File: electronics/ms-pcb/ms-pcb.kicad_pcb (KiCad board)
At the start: 2 copper layers, 112.5 x 110 mm, 16 parts, among them J1 Left motor, J2 Right motor, J3 XT60-M

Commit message: elec: start PCB layout
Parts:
- added H1: Motor_holes, footprints:Polulu_Micro_Gearmotor, F.Cu at (100.0, 95.0)
- added H2: Caster_wheel_holes, footprints:caster_wheel, F.Cu at (133.0, 51.0)
- added H3: Motor_holes, footprints:Polulu_Micro_Gearmotor, F.Cu at (167.0, 95.0)
- added H4: Caster_wheel_holes, footprints:caster_wheel, F.Cu at (133.0, 139.0)
- added S1: PTS526_SMG15_SMTR2_LFS, footprints:SW_PTS526_SMG15_SMTR2_LFS, F.Cu at (135.0, 95.0)
- added U1: ESP32-S3-DEVKITC-1U-N8R2, footprints:XCVR_ESP32-S3-DEVKITC-1U-N8R2, F.Cu at (134.0, 73.0)
- added U2: GY-521, footprints:GY-521, B.Cu at (106.0, 122.0)
- LS1, R2, R5: moved to B.Cu
- VL53L1X1: value ToF distance sensor -> Left; footprint Connector_PinHeader_2.54mm:PinHeader_1x06_P2.54mm_Horizontal -> footprints:TinyTronics_VL53L1X
- VL53L1X2: value ToF distance sensor -> Front-right; footprint Connector_PinHeader_2.54mm:PinHeader_1x06_P2.54mm_Horizontal -> footprints:TinyTronics_VL53L1X
- VL53L1X3: value ToF distance sensor -> Front-left; footprint Connector_PinHeader_2.54mm:PinHeader_1x06_P2.54mm_Horizontal -> footprints:TinyTronics_VL53L1X
- VL53L1X4: value ToF distance sensor -> Right; footprint Connector_PinHeader_2.54mm:PinHeader_1x06_P2.54mm_Horizontal -> footprints:TinyTronics_VL53L1X
- VL53L1X5: value ToF distance sensor -> Front; footprint Connector_PinHeader_2.54mm:PinHeader_1x06_P2.54mm_Horizontal -> footprints:TinyTronics_VL53L1X
- moved J3 259.3 mm to (171.0, 122.0), turned to -90 degrees
- moved J2 239.3 mm to (160.0, 108.0), turned to 180 degrees
- moved VL53L1X2 237.3 mm to (178.6, 70.4), turned to -135 degrees
- moved D1 217.6 mm to (140.5, 109.0)
- moved R3 214.2 mm to (141.0, 103.0)
- moved VL53L1X4 210.7 mm to (151.7, 55.4), turned to 180 degrees
- moved D2 206.6 mm to (125.5, 109.0)
- moved R4 200.1 mm to (125.5, 103.0)
- moved R2 198.4 mm to (153.0, 70.0)
- moved VL53L1X5 180.9 mm to (139.8, 46.7), turned to -90 degrees
- moved R5 176.7 mm to (153.0, 76.0), turned to 180 degrees
- moved VL53L1X3 173.7 mm to (97.7, 61.2), turned to -45 degrees
- moved R1 167.5 mm to (125.0, 96.0), turned to 180 degrees
- moved LS1 164.5 mm to (120.0, 72.0), turned to 180 degrees
- moved J1 158.2 mm to (107.0, 108.0), turned to 180 degrees
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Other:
- board outline removed

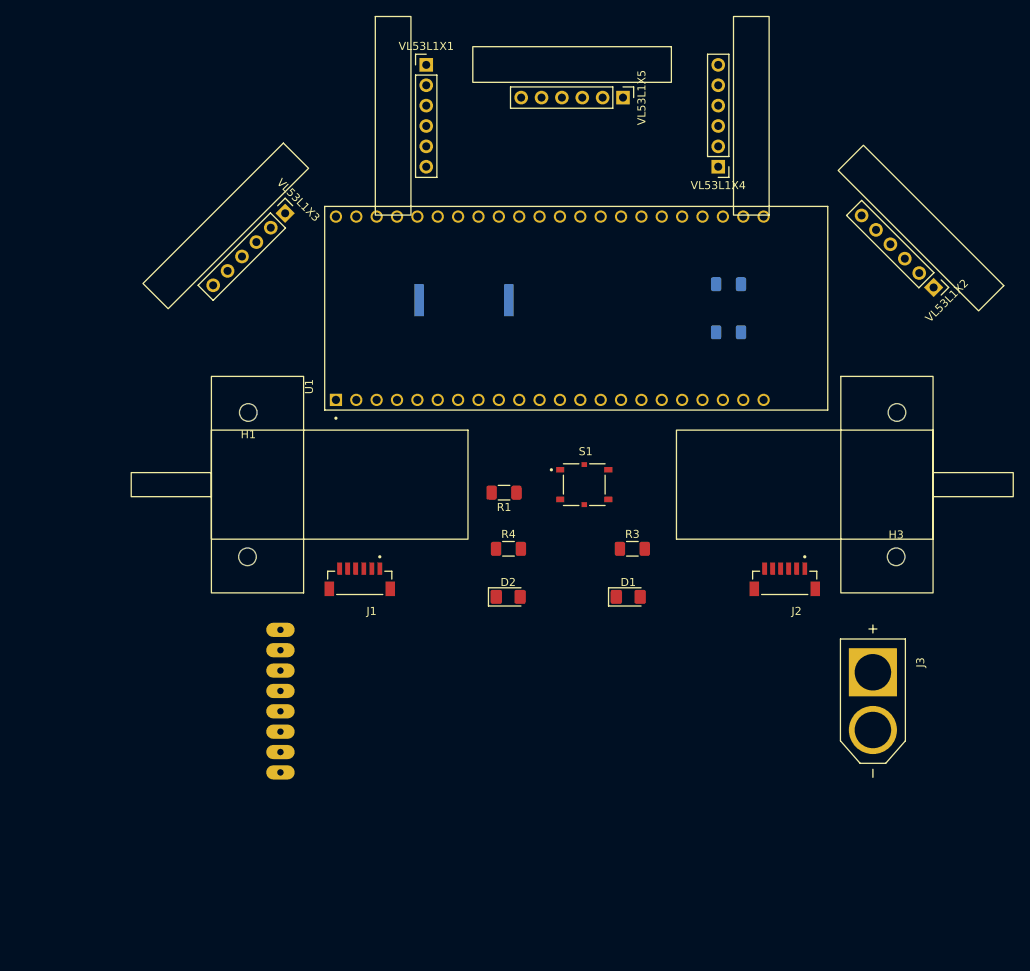
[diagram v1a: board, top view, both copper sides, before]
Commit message: elec: add more 3D and link them to footprints
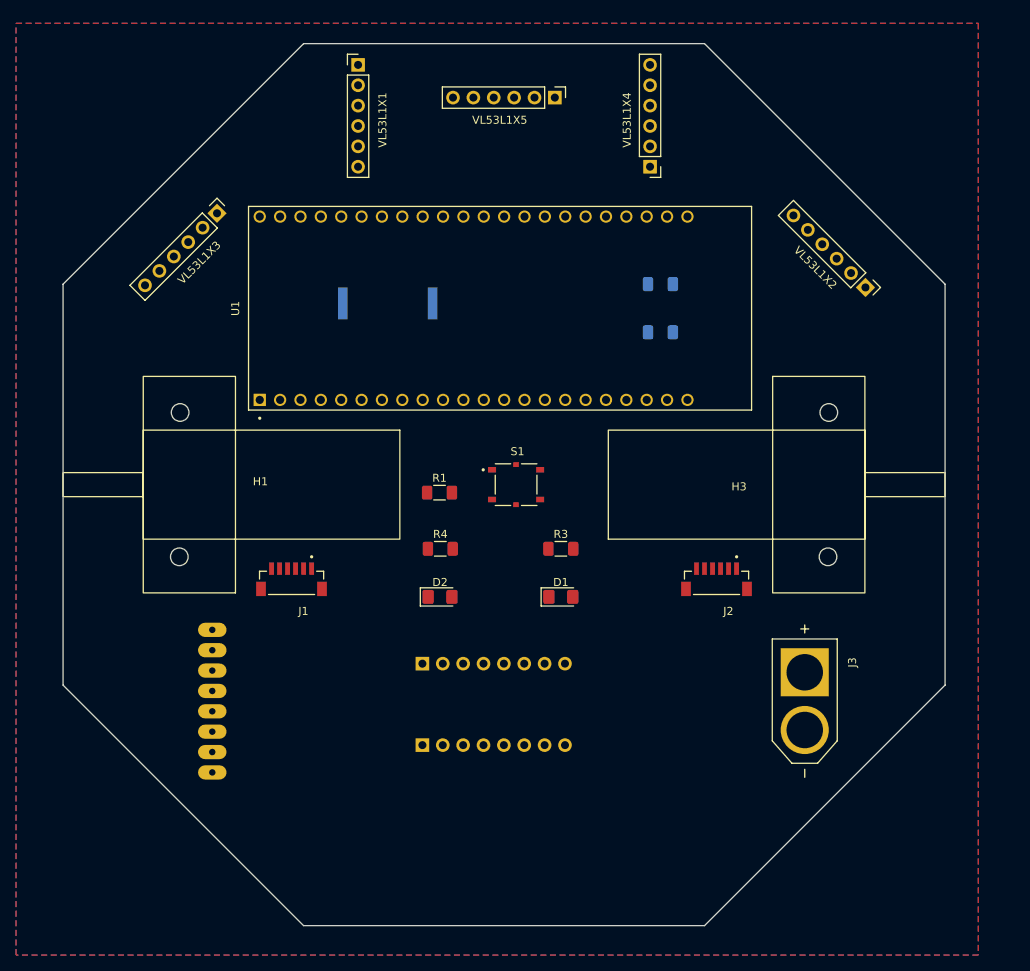
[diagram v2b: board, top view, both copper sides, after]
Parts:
- added DRV1: DRV8833, footprints:Polulu_DRV8833, B.Cu at (123.8, 122.6)
- R1: value 100k -> 20k
- moved LS1 9.52 mm to (110.5, 72.4)
- moved U1 9.50 mm to (124.5, 73.0)
- moved R3 8.92 mm to (132.1, 103.0)
- moved H3 8.50 mm to (158.5, 95.0)
- moved H1 8.50 mm to (91.5, 95.0)
- moved VL53L1X2 8.50 mm to (170.1, 70.4)
- moved VL53L1X1 8.50 mm to (106.8, 42.7)
- moved D2 8.50 mm to (117.0, 109.0)
- moved H2 8.50 mm to (124.5, 51.0)
- moved H4 8.50 mm to (124.5, 139.0)
- moved R2 8.50 mm to (144.5, 70.0)
- moved R4 8.50 mm to (117.0, 103.0)
- moved R5 8.50 mm to (144.5, 76.0)
- moved U2 8.50 mm to (97.5, 122.0)
- moved S1 8.50 mm to (126.5, 95.0)
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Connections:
- R1 pad 2: GND -> button
- R4 pad 1: +BATT -> +3.3V
- S1 pad 1: +3.3V -> button
- S1 pad 2: +3.3V -> button
- S1 pad 3: button -> GND
- S1 pad 4: button -> GND
- S1 pad G1: GND -> Net-(S1-PadG1)
- S1 pad G2: GND -> Net-(S1-PadG1)
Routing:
- added copper zone on F.Cu, net +3.3V
- added copper zone on B.Cu, net GND
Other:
- board outline added: 110 x 110 mm

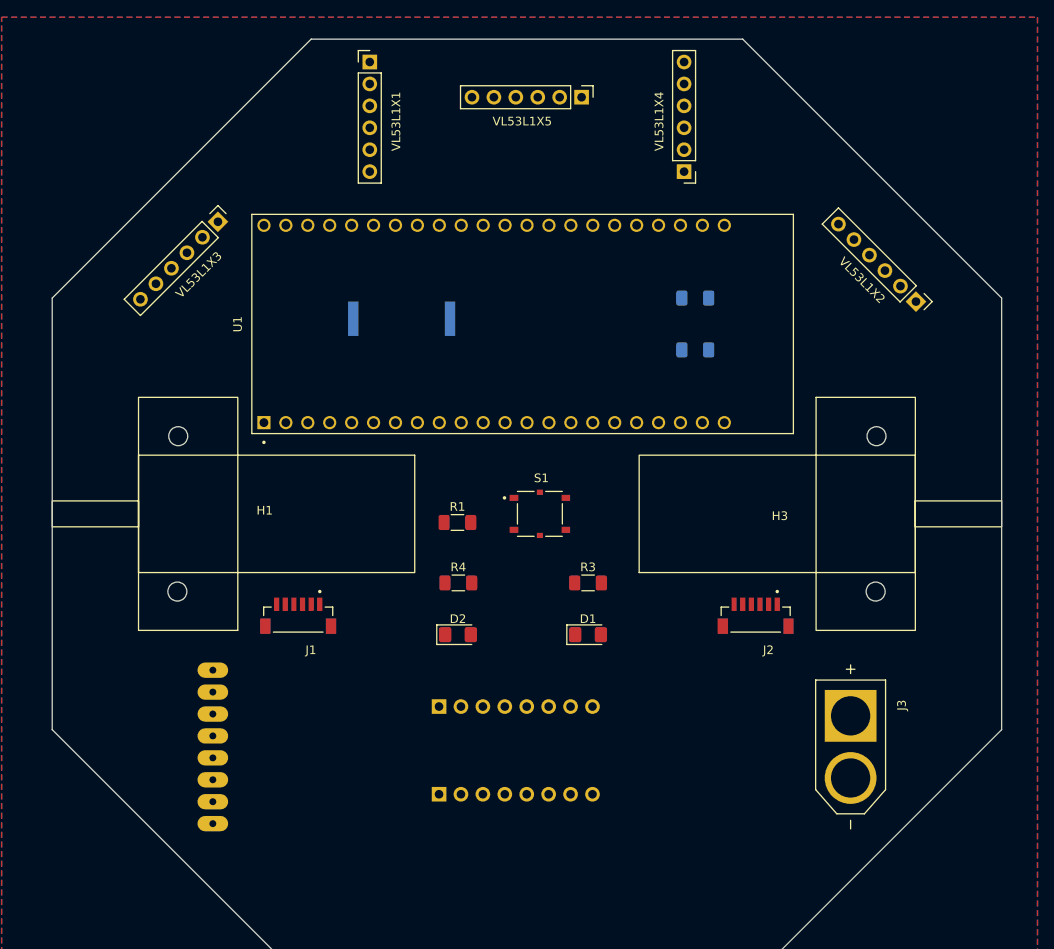
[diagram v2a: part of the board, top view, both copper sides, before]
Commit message: elec: add most 3D models
Closes: #19
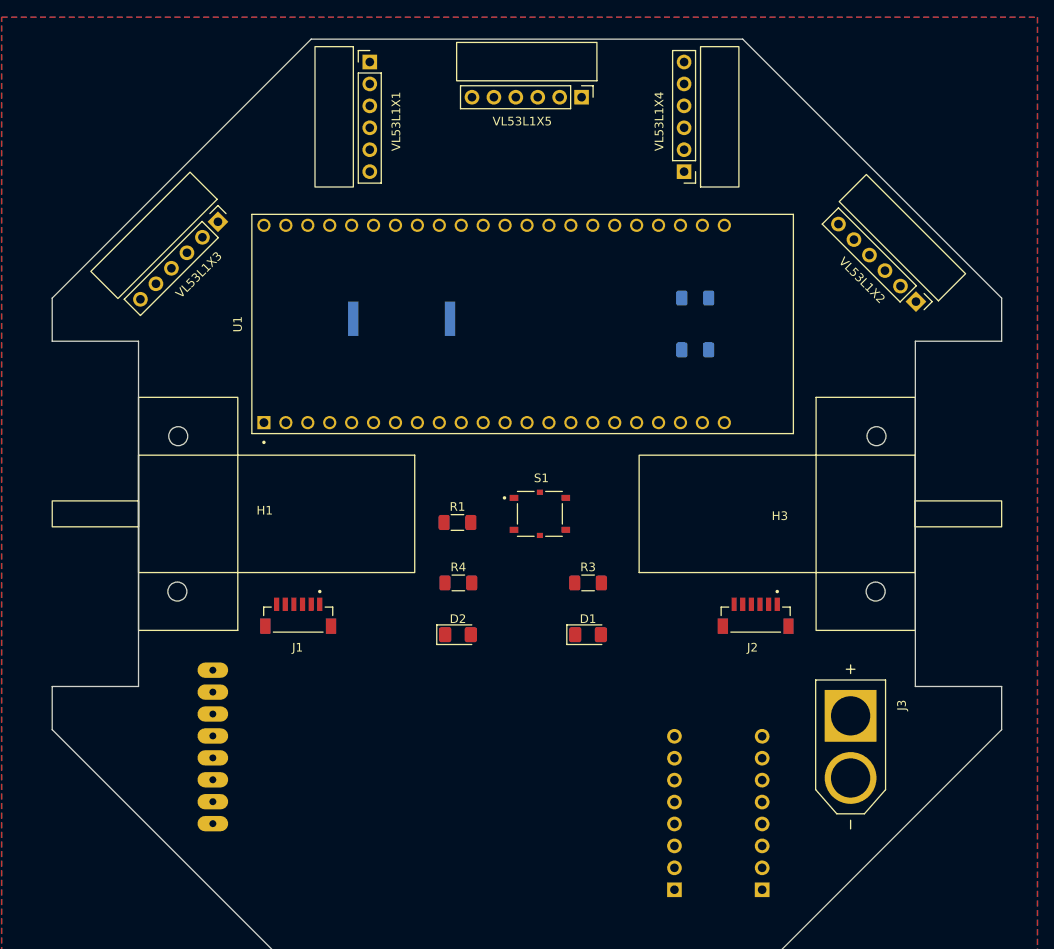
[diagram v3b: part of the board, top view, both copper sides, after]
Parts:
- moved DRV8833 24.5 mm to (147.3, 129.5), turned to 0 degrees
- renumbered DRV1 to DRV8833
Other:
- outline, holes or cut-outs redrawn

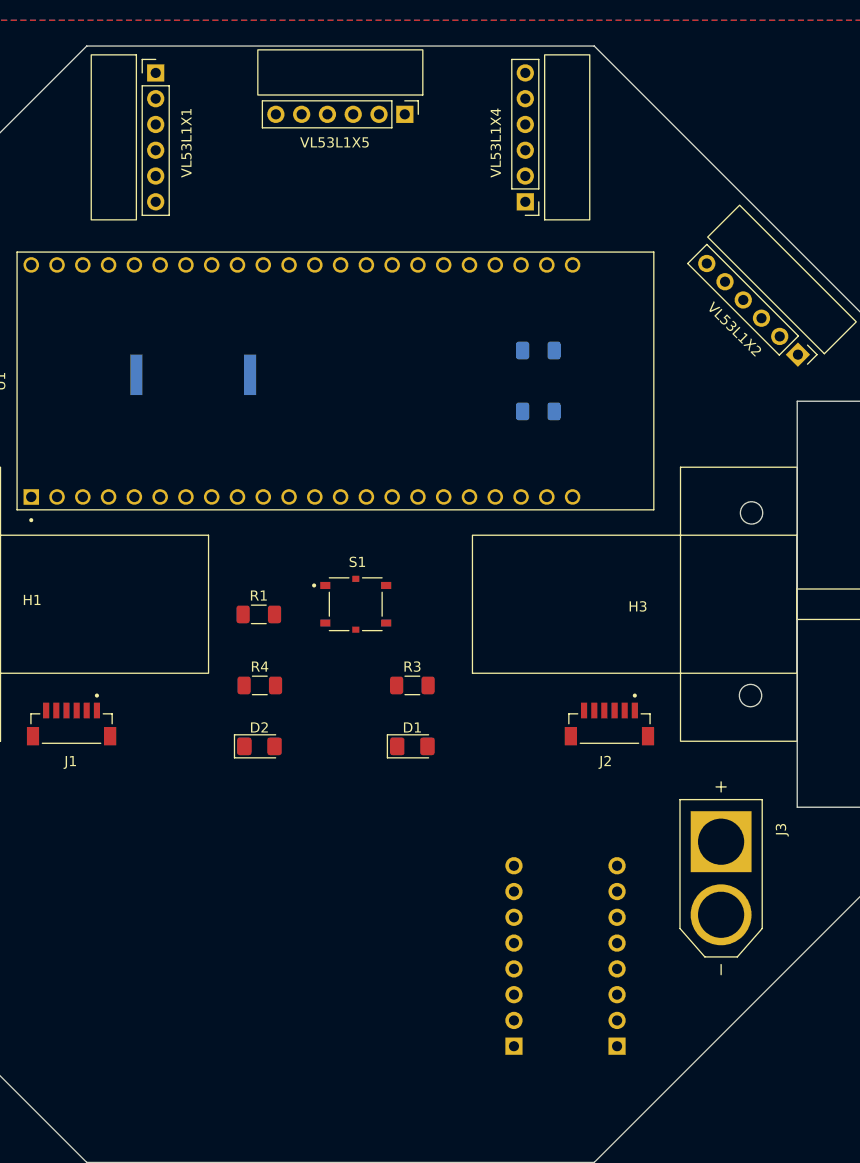
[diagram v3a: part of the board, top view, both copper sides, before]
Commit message: elec: add more 3D models and enhance layout
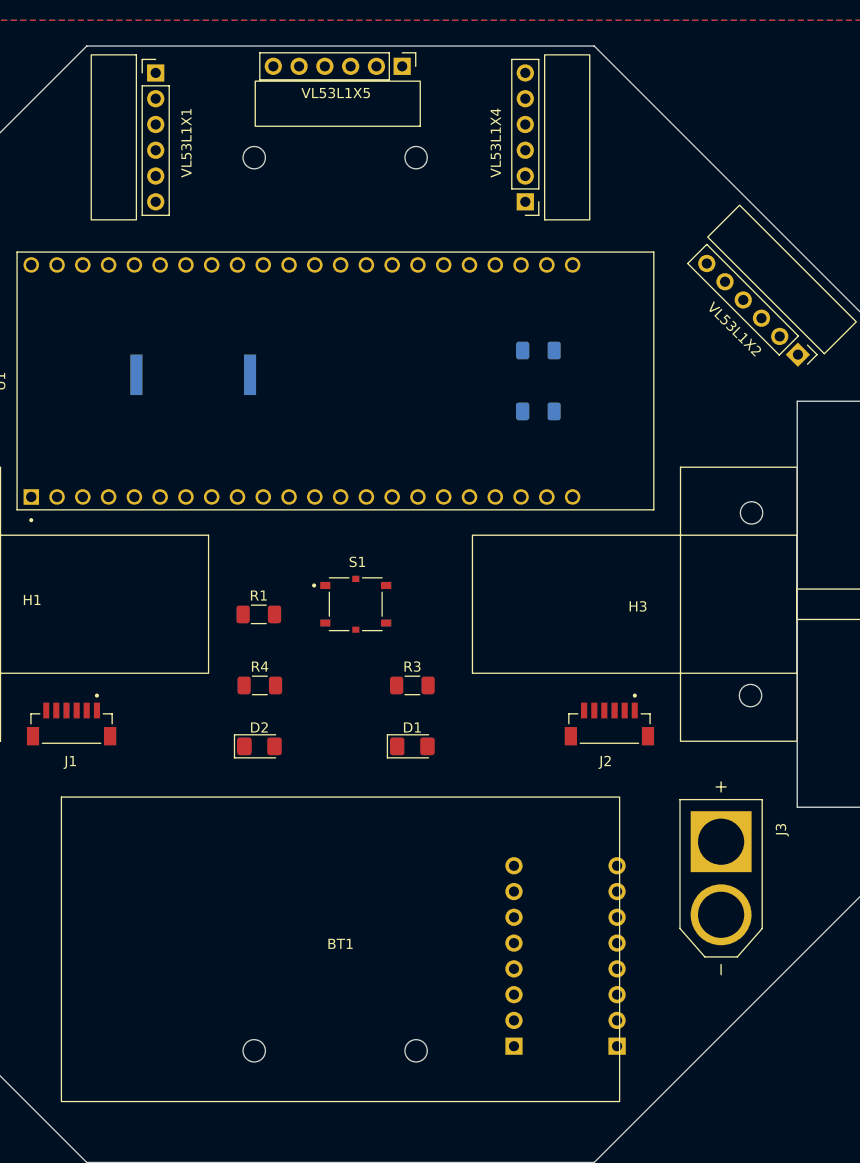
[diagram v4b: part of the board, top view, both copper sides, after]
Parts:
- added BT1: Battery, footprints:LiPo_2S1P_Battery, F.Cu at (125.0, 129.0)
- H2, H4: moved to B.Cu
- VL53L1X5: footprint footprints:TinyTronics_VL53L1X -> footprints:TinyTronics_VL53L1X_header_front
- moved VL53L1X5 4.74 mm to (131.1, 42.0)
- turned H2 to 180 degrees
- turned H4 to 180 degrees
- renumbered DRV8833 to DRV1
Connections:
- J1 pad S1: unconnected-(J1-PadS1) -> unconnected-(J1-SHIELD-PadS1)
- J1 pad S2: unconnected-(J1-PadS1) -> unconnected-(J1-SHIELD-PadS1)_0
- J2 pad S1: unconnected-(J2-PadS1) -> unconnected-(J2-SHIELD-PadS1)
- J2 pad S2: unconnected-(J2-PadS1) -> unconnected-(J2-SHIELD-PadS1)_0
